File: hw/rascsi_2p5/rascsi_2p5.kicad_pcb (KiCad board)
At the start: 2 copper layers, 65 x 56 mm, 99 parts, among them IC1 SN74LS641-1DW, IC2 SN74LS641-1DW, IC3 SN74LS641-1DW, IC4 SN74LS641-1DW, J1 Raspberry_Pi_2_3, J10 Conn_01x04_Male, J11 DNP, J2 DNP, J20 171826-4, J3 Conn_02x25_Odd_Even, J4 I2C Pinout, J5 DNP, J6 CONNFLY DB-25, J7 DNP, J8 USB_B_Micro, J9 Conn_02x25_Odd_Even, X1 Mac, X2 Dogcow, X3 Mac, X4 Dogcow, X5 Dogcow, X6 Dogcow, X7 Pi, X8 Pi

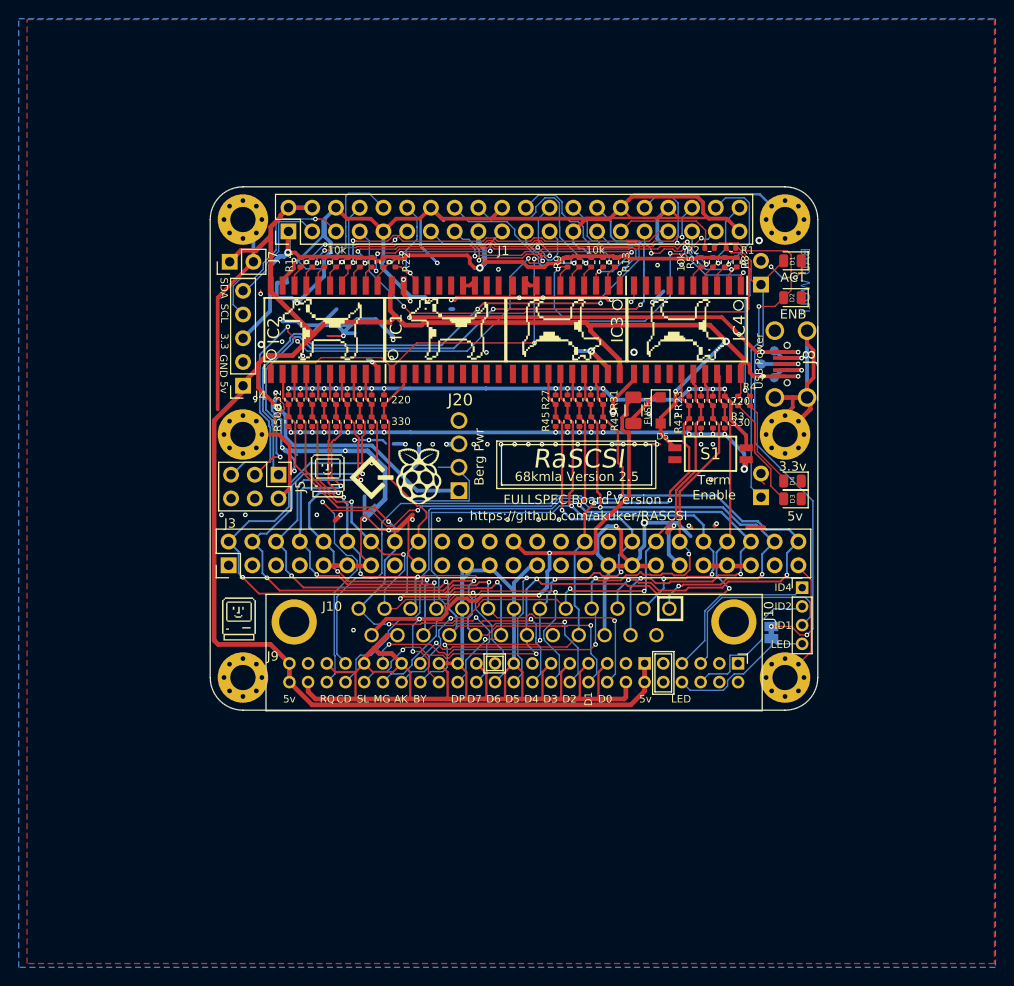
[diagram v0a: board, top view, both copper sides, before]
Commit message: Updated to Kicad 6 and modified act LED
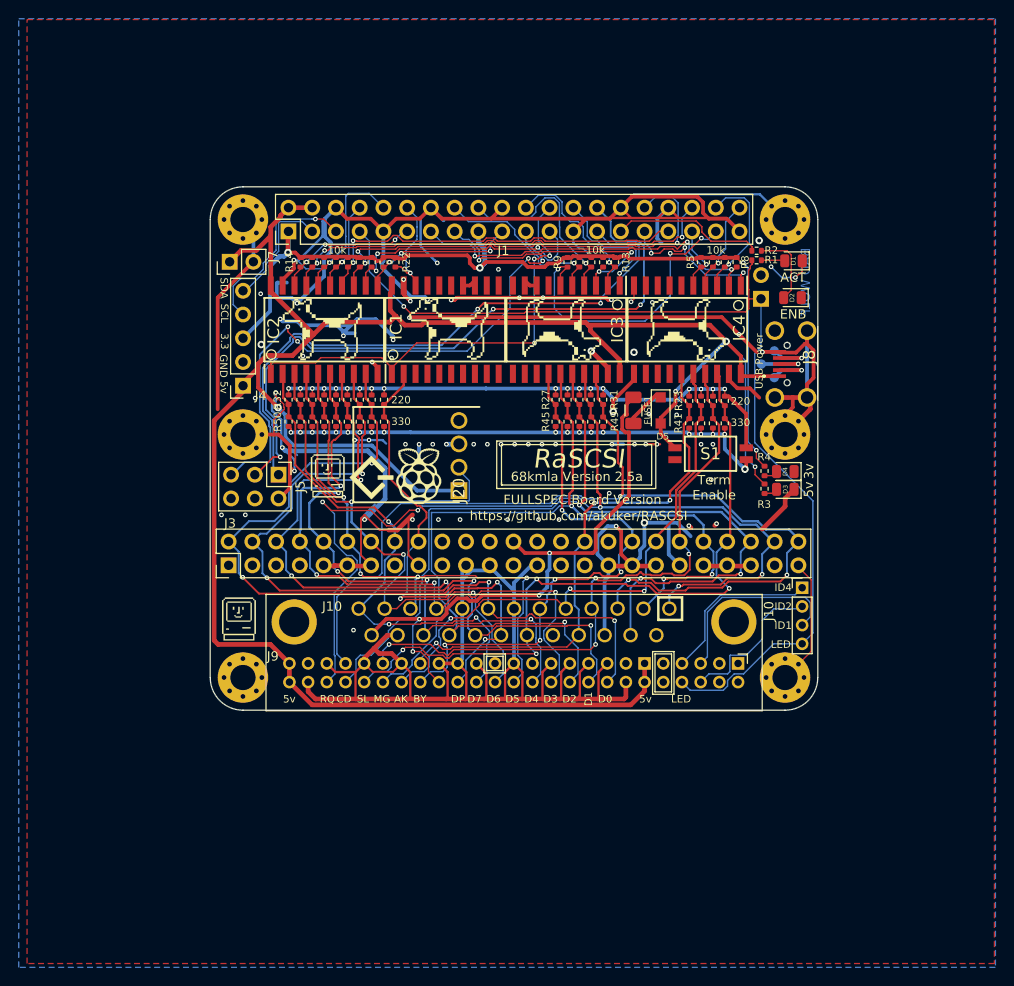
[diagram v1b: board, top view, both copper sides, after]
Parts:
- removed J11: DNP, Connector_PinHeader_2.54mm:PinHeader_1x02_P2.54mm_Horizontal
- removed JP1: SolderJumper_2_Bridged, Jumper:SolderJumper-2_P1.3mm_Bridged_Pad1.0x1.5mm
- moved R3 9.82 mm to (233.8, 74.8)
- moved R4 7.65 mm to (233.8, 72.9)
- moved R2 5.04 mm to (233.0, 49.3)
- moved R1 3.05 mm to (233.0, 50.4)
- moved J2 1.52 mm to (233.4, 54.5)
- moved D4 1.27 mm to (236.0, 73.0)
- moved D3 1.27 mm to (236.0, 74.9)
- moved D1 0.11 mm to (236.9, 50.4)
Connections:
- net EXT-ENB-LED renamed Net-(D2-Pad2)
- D1 pad 2: EXT-ACT-LED -> Net-(D1-Pad2)
- J1 pad 7: PI-ACT -> PB_LED_Pin
- J2 pad 1: EXT-ACT-LED -> PB_LED_Pin
- J20 pad 4: (no net) -> unconnected-(J20-Pad4)
- J3 pad 25: (no net) -> unconnected-(J3-Pad25)
- J3 pad 34: (no net) -> unconnected-(J3-Pad34)
- J9 pad 1: (no net) -> unconnected-(J9-Pad1)
- J9 pad 10: (no net) -> unconnected-(J9-Pad10)
- J9 pad 2: (no net) -> unconnected-(J9-Pad2)
- J9 pad 27: (no net) -> unconnected-(J9-Pad27)
- J9 pad 3: (no net) -> unconnected-(J9-Pad3)
- J9 pad 4: (no net) -> unconnected-(J9-Pad4)
- J9 pad 9: (no net) -> unconnected-(J9-Pad9)
- R1 pad 1: PI-ACT -> PB_LED_Pin
- R1 pad 2: EXT-ACT-LED -> Net-(D1-Pad2)
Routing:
- net PB_LED_Pin: track 16.6 -> 110.0 mm, vias 0 -> 1
- net PI-ACT: track 56.2 -> 0.00 mm, vias 1 -> 0
- net EXT-ACT-LED: track 54.3 -> 0.00 mm, vias 2 -> 0
- net GND: track 636.8 -> 605.3 mm, vias 83 -> 71
- net Net-(D2-Pad2): track 38.1 -> 8.30 mm, vias 1 -> 0
- net Net-(D3-Pad2): track 12.0 -> 1.11 mm
- net +5V: track 232.8 -> 243.4 mm, vias 5 -> 4
- net Net-(D4-Pad2): track 9.56 -> 1.23 mm
- net +3V3: track 87.5 -> 95.0 mm
- net DBG_LED: track 11.9 -> 16.4 mm
- net /TERM_GND: track 69.1 -> 65.0 mm
- net Net-(D1-Pad2): track 0.00 -> 2.52 mm
- net PI-D3: track 42.8 -> 40.7 mm
- net PI-REQ: track 28.7 -> 28.0 mm
- net C-DP: track 53.4 -> 52.8 mm
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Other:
- net class Default removed
- board text added: "3v"
- board text added: "68kmla Version 2.5a"
- board text removed: "+12v"
- board text removed: "3.3v"
- board text removed: "68kmla Version 2.5"
- board text removed: "ACT LED"
- board text removed: "BERG PWR CONNECTOR"
- board text removed: "Berg Pwr"
- board text removed: "ENB LED"

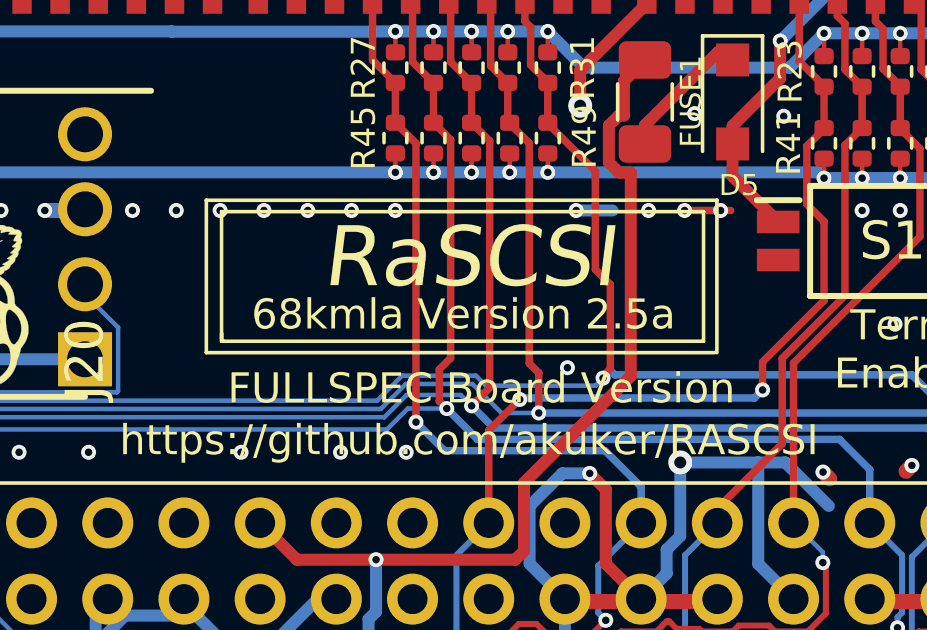
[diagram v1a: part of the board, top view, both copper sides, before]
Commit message: Regenerated Gerber files to fix drill placement. Added CE logo
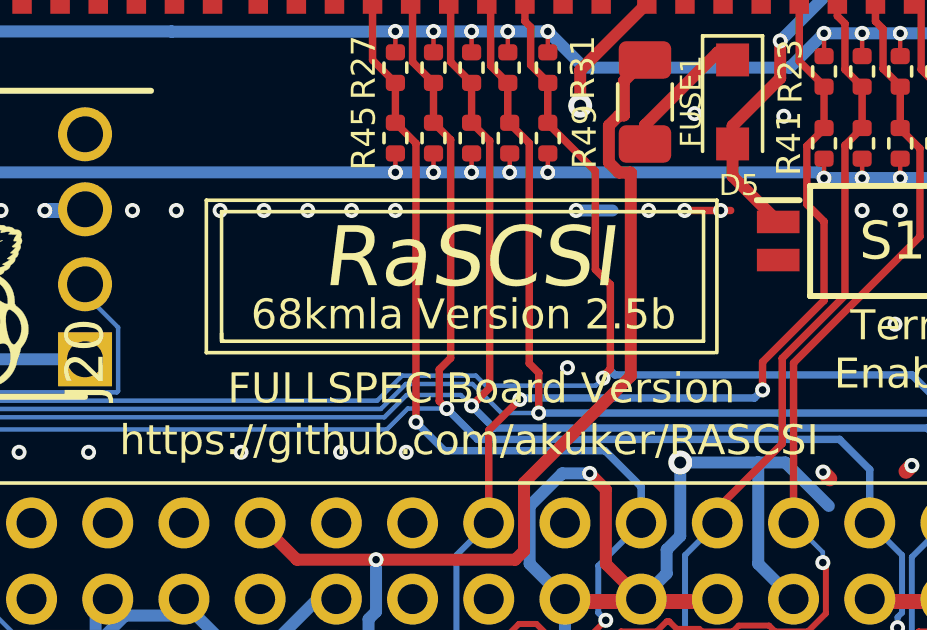
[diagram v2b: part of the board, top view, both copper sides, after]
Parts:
- added REF**: CE-Logo_8.5x6mm_SilkScreen, Symbol:CE-Logo_8.5x6mm_SilkScreen, B.Cu at (223.6, 55.9)
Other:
- board text added: "68kmla Version 2.5b"
- board text removed: "68kmla Version 2.5a"
